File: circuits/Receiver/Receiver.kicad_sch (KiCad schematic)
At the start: 33 parts, among them J1 ORA. . .12V, J10 DI, J11 GND, J2 ORA___12V, J3 GRN. . .12V, J4 BLU___A, J5 BLU. . .B, J6 GRN___GND, J7 BRN. . .GND, J8 BRN___GND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

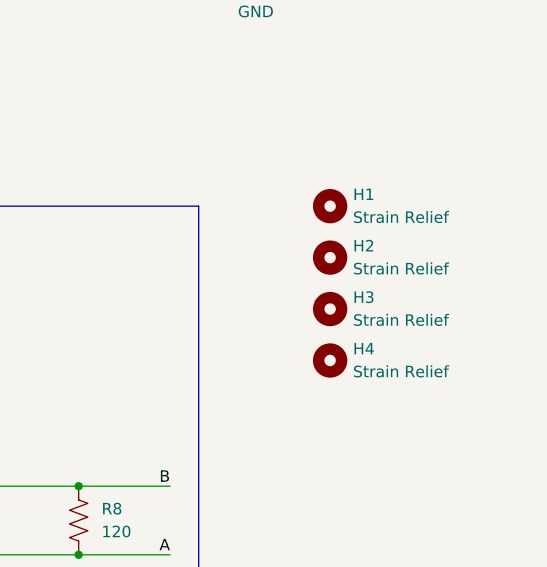
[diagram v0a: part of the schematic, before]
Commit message: Use zipties for strain relief on cables
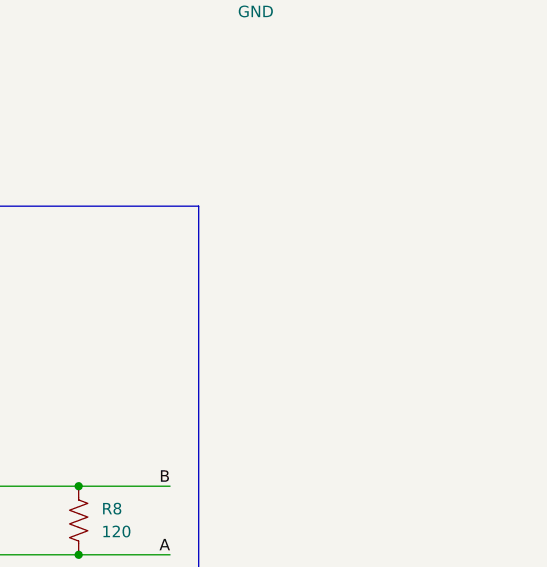
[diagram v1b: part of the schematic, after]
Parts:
- removed H1, H3: Strain Relief, MountingHole:MountingHole_4mm, symbol Mechanical:MountingHole
- removed H2, H4: Strain Relief, MountingHole:MountingHole_6mm, symbol Mechanical:MountingHole
- J10, J11, J9: footprint TestPoint:TestPoint_Pad_2.5x2.5mm -> Connector_Wire:SolderWire-1sqmm_1x01_D1.4mm_OD2.7mm
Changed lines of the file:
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@@
     (pin "3")
-  )
-  (symbol (lib_id "Mechanical:MountingHole") (at 196.215 73.025 0) (unit 1)
-    (in_bom yes) (on_board yes) (fields_autoplaced)
-    (property "Reference" "H2" (id 0) (at 198.755 71.7549 0)
-      (effects (font (size 1.27 1.27)) (justify left))
-    )
-    (property "Value" "Strain Relief" (id 1) (at 198.755 74.2949 0)
-      (effects (font (size 1.27 1.27)) (justify left))
-    )
-    (property "Footprint" "MountingHole:MountingHole_6mm" (id 2) (at 196.215 73.025 0)
-      (effects (font (size 1.27 1.27)) hide)
-    )
-    (property "Datasheet" "~" (id 3) (at 196.215 73.025 0)
-      (effects (font (size 1.27 1.27)) hide)
-    )
   )
   (symbol (lib_id "power:GND") (at 30.48 55.88 0) (unit 1)
@@
     )
     (pin "1")
-  )
-  (symbol (lib_id "Mechanical:MountingHole") (at 196.215 67.31 0) (unit 1)
-    (in_bom yes) (on_board yes) (fields_autoplaced)
-    (property "Reference" "H1" (id 0) (at 198.755 66.0399 0)
-      (effects (font (size 1.27 1.27)) (justify left))
-    )
-    (property "Value" "Strain Relief" (id 1) (at 198.755 68.5799 0)
-      (effects (font (size 1.27 1.27)) (justify left))
-    )
-    (property "Footprint" "MountingHole:MountingHole_4mm" (id 2) (at 196.215 67.31 0)
-      (effects (font (size 1.27 1.27)) hide)
-    )
-    (property "Datasheet" "~" (id 3) (at 196.215 67.31 0)
-      (effects (font (size 1.27 1.27)) hide)
-    )
   )
   (symbol (lib_id "Connector:Conn_01x01_Male") (at 40.005 52.705 180) (unit 1)
@@
     (property "Reference" "J11" (id 0) (at 205.105 40.64 0))
     (property "Value" "GND" (id 1) (at 215.9 40.64 0))
-    (property "Footprint" "TestPoint:TestPoint_Pad_2.5x2.5mm" (id 2) (at 201.93 40.64 0)
+    (property "Footprint" "Connector_Wire:SolderWire-1sqmm_1x01_D1.4mm_OD2.7mm" (id 2) (at 201.93 40.64 0)
       (effects (font (size 1.27 1.27)) hide)
     )
@@
     (property "Reference" "J9" (id 0) (at 205.105 35.56 0))
     (property "Value" "12V" (id 1) (at 215.9 35.56 0))
-    (property "Footprint" "TestPoint:TestPoint_Pad_2.5x2.5mm" (id 2) (at 201.93 35.56 0)
+    (property "Footprint" "Connector_Wire:SolderWire-1sqmm_1x01_D1.4mm_OD2.7mm" (id 2) (at 201.93 35.56 0)
       (effects (font (size 1.27 1.27)) hide)
     )
@@
     )
     (pin "1")
-  )
-  (symbol (lib_id "Mechanical:MountingHole") (at 196.215 84.455 0) (unit 1)
-    (in_bom yes) (on_board yes) (fields_autoplaced)
-    (property "Reference" "H4" (id 0) (at 198.755 83.1849 0)
-      (effects (font (size 1.27 1.27)) (justify left))
-    )
-    (property "Value" "Strain Relief" (id 1) (at 198.755 85.7249 0)
-      (effects (font (size 1.27 1.27)) (justify left))
-    )
-    (property "Footprint" "MountingHole:MountingHole_6mm" (id 2) (at 196.215 84.455 0)
-      (effects (font (size 1.27 1.27)) hide)
-    )
-    (property "Datasheet" "~" (id 3) (at 196.215 84.455 0)
-      (effects (font (size 1.27 1.27)) hide)
-    )
-  )
-  (symbol (lib_id "Mechanical:MountingHole") (at 196.215 78.74 0) (unit 1)
-    (in_bom yes) (on_board yes) (fields_autoplaced)
-    (property "Reference" "H3" (id 0) (at 198.755 77.4699 0)
-      (effects (font (size 1.27 1.27)) (justify left))
-    )
-    (property "Value" "Strain Relief" (id 1) (at 198.755 80.0099 0)
-      (effects (font (size 1.27 1.27)) (justify left))
-    )
-    (property "Footprint" "MountingHole:MountingHole_4mm" (id 2) (at 196.215 78.74 0)
-      (effects (font (size 1.27 1.27)) hide)
-    )
-    (property "Datasheet" "~" (id 3) (at 196.215 78.74 0)
-      (effects (font (size 1.27 1.27)) hide)
-    )
   )
   (symbol (lib_id "Connector:Conn_01x01_Male") (at 40.005 55.88 180) (unit 1)
@@
     (property "Reference" "J10" (id 0) (at 205.105 38.1 0))
     (property "Value" "DI" (id 1) (at 215.9 38.1 0))
-    (property "Footprint" "TestPoint:TestPoint_Pad_2.5x2.5mm" (id 2) (at 201.93 38.1 0)
+    (property "Footprint" "Connector_Wire:SolderWire-1sqmm_1x01_D1.4mm_OD2.7mm" (id 2) (at 201.93 38.1 0)
       (effects (font (size 1.27 1.27)) hide)
     )
@@
       (reference "D1") (unit 1) (value "LED") (footprint "LED_SMD:LED_0805_2012Metric")
     )
-    (path "/0e62283a-6cc9-41a2-8a34-651f9acda105"
-      (reference "H1") (unit 1) (value "Strain Relief") (footprint "MountingHole:MountingHole_4mm")
-    )
-    (path "/075f1041-1c39-464b-82c2-6a4e8714a197"
-      (reference "H2") (unit 1) (value "Strain Relief") (footprint "MountingHole:MountingHole_6mm")
-    )
-    (path "/7405c8af-2dd9-442e-b1bc-358e49cb7699"
-      (reference "H3") (unit 1) (value "Strain Relief") (footprint "MountingHole:MountingHole_4mm")
-    )
-    (path "/707cdb84-ee7e-41e9-a0d0-98a07dd4db1e"
-      (reference "H4") (unit 1) (value "Strain Relief") (footprint "MountingHole:MountingHole_6mm")
-    )
     (path "/d21f9f13-8f39-4c32-8940-596c75d14d3f"
       (reference "J1") (unit 1) (value "ORA. . .12V") (footprint "Connector_Wire:SolderWire-0.25sqmm_1x01_D0.65mm_OD1.7mm")
@@
     )
     (path "/6dbbdef5-0ae7-41bf-be4c-f967c719f1d3"
-      (reference "J9") (unit 1) (value "12V") (footprint "TestPoint:TestPoint_Pad_2.5x2.5mm")
+      (reference "J9") (unit 1) (value "12V") (footprint "Connector_Wire:SolderWire-1sqmm_1x01_D1.4mm_OD2.7mm")
     )
     (path "/a524b17a-5fd1-4168-b7b6-ae80a944e6d2"
-      (reference "J10") (unit 1) (value "DI") (footprint "TestPoint:TestPoint_Pad_2.5x2.5mm")
+      (reference "J10") (unit 1) (value "DI") (footprint "Connector_Wire:SolderWire-1sqmm_1x01_D1.4mm_OD2.7mm")
     )
     (path "/1c926daf-5c58-40db-be92-ef7ff90648a3"
-      (reference "J11") (unit 1) (value "GND") (footprint "TestPoint:TestPoint_Pad_2.5x2.5mm")
+      (reference "J11") (unit 1) (value "GND") (footprint "Connector_Wire:SolderWire-1sqmm_1x01_D1.4mm_OD2.7mm")
     )
     (path "/9f7c9c77-7ea1-4166-8350-df4fe1e7a5bb"

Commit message: 1.0 sent to production
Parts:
- added H1, H2: JLCPCB Tooling, Joels KiCad Footprint Library:JCLPCB_Tooling_Hole, symbol Mechanical:MountingHole
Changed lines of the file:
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@@
     (pin "1")
+  )
+  (symbol (lib_id "Mechanical:MountingHole") (at 214.63 93.98 0) (unit 1)
+    (in_bom yes) (on_board yes) (fields_autoplaced)
+    (property "Reference" "H2" (id 0) (at 217.17 92.7099 0)
+      (effects (font (size 1.27 1.27)) (justify left))
+    )
+    (property "Value" "JLCPCB Tooling" (id 1) (at 217.17 95.2499 0)
+      (effects (font (size 1.27 1.27)) (justify left))
+    )
+    (property "Footprint" "Joels KiCad Footprint Library:JCLPCB_Tooling_Hole" (id 2) (at 214.63 93.98 0)
+      (effects (font (size 1.27 1.27)) hide)
+    )
+    (property "Datasheet" "~" (id 3) (at 214.63 93.98 0)
+      (effects (font (size 1.27 1.27)) hide)
+    )
   )
   (symbol (lib_id "Connector:Conn_01x01_Male") (at 201.93 40.64 180) (unit 1)
@@
     (pin "1")
   )
+  (symbol (lib_id "Mechanical:MountingHole") (at 214.63 85.09 0) (unit 1)
+    (in_bom yes) (on_board yes) (fields_autoplaced)
+    (property "Reference" "H1" (id 0) (at 217.17 83.8199 0)
+      (effects (font (size 1.27 1.27)) (justify left))
+    )
+    (property "Value" "JLCPCB Tooling" (id 1) (at 217.17 86.3599 0)
+      (effects (font (size 1.27 1.27)) (justify left))
+    )
+    (property "Footprint" "Joels KiCad Footprint Library:JCLPCB_Tooling_Hole" (id 2) (at 214.63 85.09 0)
+      (effects (font (size 1.27 1.27)) hide)
+    )
+    (property "Datasheet" "~" (id 3) (at 214.63 85.09 0)
+      (effects (font (size 1.27 1.27)) hide)
+    )
+  )
   (symbol (lib_id "Device:C_Small") (at 78.74 44.45 0) (unit 1)
     (in_bom yes) (on_board yes) (fields_autoplaced)
@@
       (reference "D1") (unit 1) (value "LED") (footprint "LED_SMD:LED_0805_2012Metric")
     )
+    (path "/db0e557c-8a08-4691-a171-5438a9008036"
+      (reference "H1") (unit 1) (value "JLCPCB Tooling") (footprint "Joels KiCad Footprint Library:JCLPCB_Tooling_Hole")
+    )
+    (path "/1757e2b8-fd02-49ec-9bcc-55c792b425a6"
+      (reference "H2") (unit 1) (value "JLCPCB Tooling") (footprint "Joels KiCad Footprint Library:JCLPCB_Tooling_Hole")
+    )
     (path "/d21f9f13-8f39-4c32-8940-596c75d14d3f"
